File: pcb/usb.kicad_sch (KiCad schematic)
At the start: 9 parts, among them J3 918-418K2023S40001, U5 CH340N

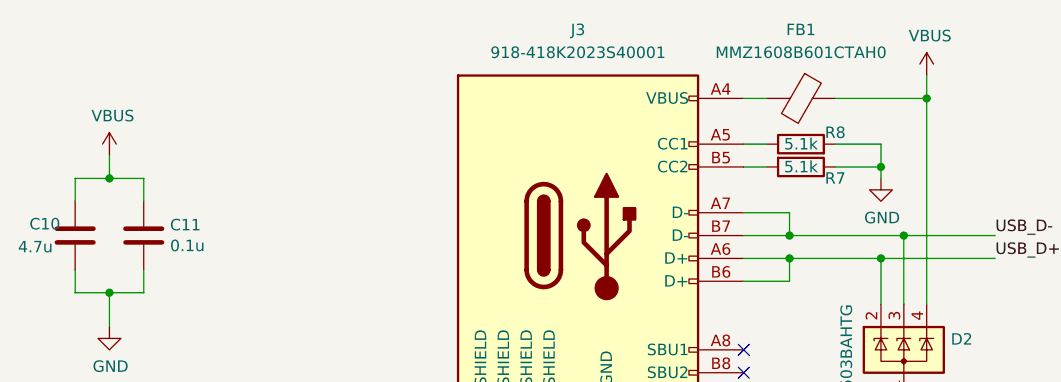
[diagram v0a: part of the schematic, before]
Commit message: Fix ERC warnings
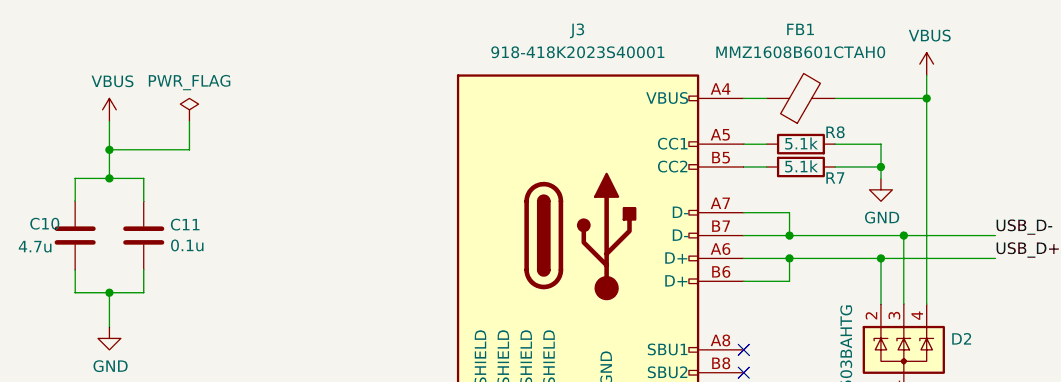
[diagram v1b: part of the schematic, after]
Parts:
- removed FB1: MMZ1608B601CTAH0, Capacitor_SMD:C_0603_1608Metric, symbol ultramote-rescue:Ferrite_Bead-Device
- added FB1: MMZ1608B601CTAH0, Capacitor_SMD:C_0603_1608Metric, symbol Device:FerriteBead
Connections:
- net VBUS: now also FB1.2
- net at J3.A4 (VBUS), J3.A9 (VBUS), J3.B4 (VBUS)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: now also FB1.1
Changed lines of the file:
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@@
   (junction (at 195.58 95.25) (diameter 0) (color 0 0 0 0)
+  )
+  (junction (at 59.055 66.675) (diameter 0) (color 0 0 0 0)
   )
   (junction (at 149.86 60.96) (diameter 0) (color 0 0 0 0)
@@
     (stroke (width 0) (type default) (color 0 0 0 0))
   )
-  (wire (pts (xy 59.055 67.31) (xy 59.055 69.85))
+  (wire (pts (xy 59.055 63.5) (xy 59.055 66.675))
     (stroke (width 0) (type default) (color 0 0 0 0))
   )
@@
     (stroke (width 0) (type default) (color 0 0 0 0))
   )
+  (wire (pts (xy 59.055 66.675) (xy 59.055 69.85))
+    (stroke (width 0) (type default) (color 0 0 0 0))
+  )
+  (wire (pts (xy 67.945 66.675) (xy 59.055 66.675))
+    (stroke (width 0) (type default) (color 0 0 0 0))
+  )
   (wire (pts (xy 185.42 82.55) (xy 182.88 82.55))
     (stroke (width 0) (type default) (color 0 0 0 0))
@@
   )
   (wire (pts (xy 134.62 73.66) (xy 134.62 76.2))
+    (stroke (width 0) (type default) (color 0 0 0 0))
+  )
+  (wire (pts (xy 67.945 63.5) (xy 67.945 66.675))
     (stroke (width 0) (type default) (color 0 0 0 0))
   )
@@
     (pin "1")
   )
-  (symbol (lib_id "ultramote-rescue:Ferrite_Bead-Device") (at 135.89 60.96 270) (unit 1)
-    (in_bom yes) (on_board yes)
-    (property "Reference" "FB1" (id 0) (at 135.89 53.34 90))
-    (property "Value" "MMZ1608B601CTAH0" (id 1) (at 135.89 55.88 90))
-    (property "Footprint" "Capacitor_SMD:C_0603_1608Metric" (id 2) (at 135.89 59.182 90)
-      (effects (font (size 1.27 1.27)) hide)
-    )
-    (property "Datasheet" "~" (id 3) (at 135.89 60.96 0)
-      (effects (font (size 1.27 1.27)) hide)
-    )
-    (property "LCSC Part Number" "C97120" (id 4) (at 135.89 60.96 0)
-      (effects (font (size 1.27 1.27)) hide)
-    )
-    (property "Manufacturer Part Number" "MMZ1608B601CTAH0" (id 5) (at 135.89 60.96 0)
-      (effects (font (size 1.27 1.27)) hide)
-    )
-    (pin "1")
-    (pin "2")
-  )
   (symbol (lib_id "Device:C") (at 62.865 76.2 0) (unit 1)
     (in_bom yes) (on_board yes)
@@
     (pin "2")
   )
-  (symbol (lib_id "power:VBUS") (at 59.055 67.31 0) (unit 1)
-    (in_bom yes) (on_board yes)
-    (property "Reference" "#PWR033" (id 0) (at 59.055 71.12 0)
-      (effects (font (size 1.27 1.27)) hide)
-    )
-    (property "Value" "VBUS" (id 1) (at 59.436 62.9158 0))
-    (property "Footprint" "" (id 2) (at 59.055 67.31 0)
-      (effects (font (size 1.27 1.27)) hide)
-    )
-    (property "Datasheet" "" (id 3) (at 59.055 67.31 0)
+  (symbol (lib_id "power:VBUS") (at 59.055 63.5 0) (unit 1)
+    (in_bom yes) (on_board yes)
+    (property "Reference" "#PWR033" (id 0) (at 59.055 67.31 0)
+      (effects (font (size 1.27 1.27)) hide)
+    )
+    (property "Value" "VBUS" (id 1) (at 59.436 59.1058 0))
+    (property "Footprint" "" (id 2) (at 59.055 63.5 0)
+      (effects (font (size 1.27 1.27)) hide)
+    )
+    (property "Datasheet" "" (id 3) (at 59.055 63.5 0)
       (effects (font (size 1.27 1.27)) hide)
     )
@@
     )
     (property "Datasheet" "" (id 3) (at 149.86 58.42 0)
+      (effects (font (size 1.27 1.27)) hide)
+    )
+    (pin "1")
+  )
+  (symbol (lib_id "power:PWR_FLAG") (at 67.945 63.5 0) (unit 1)
+    (in_bom yes) (on_board yes)
+    (property "Reference" "#FLG0102" (id 0) (at 67.945 61.595 0)
+      (effects (font (size 1.27 1.27)) hide)
+    )
+    (property "Value" "PWR_FLAG" (id 1) (at 67.945 59.055 0))
+    (property "Footprint" "" (id 2) (at 67.945 63.5 0)
+      (effects (font (size 1.27 1.27)) hide)
+    )
+    (property "Datasheet" "~" (id 3) (at 67.945 63.5 0)
       (effects (font (size 1.27 1.27)) hide)
     )
@@
       (effects (font (size 1.27 1.27)) hide)
     )
+    (pin "1")
+    (pin "2")
+  )
+  (symbol (lib_id "Device:FerriteBead") (at 135.89 60.96 90) (unit 1)
+    (in_bom yes) (on_board yes) (fields_autoplaced)
+    (property "Reference" "FB1" (id 0) (at 135.8392 53.34 90))
+    (property "Value" "MMZ1608B601CTAH0" (id 1) (at 135.8392 55.88 90))
+    (property "Footprint" "Capacitor_SMD:C_0603_1608Metric" (id 2) (at 135.89 62.738 90)
+      (effects (font (size 1.27 1.27)) hide)
+    )
+    (property "Datasheet" "~" (id 3) (at 135.89 60.96 0)
+      (effects (font (size 1.27 1.27)) hide)
+    )
+    (property "LCSC Part Number" "C97120" (id 4) (at 135.89 60.96 0)
+      (effects (font (size 1.27 1.27)) hide)
+    )
+    (property "Manufacturer Part Number" "MMZ1608B601CTAH0" (id 5) (at 135.89 60.96 0)
+      (effects (font (size 1.27 1.27)) hide)
+    )

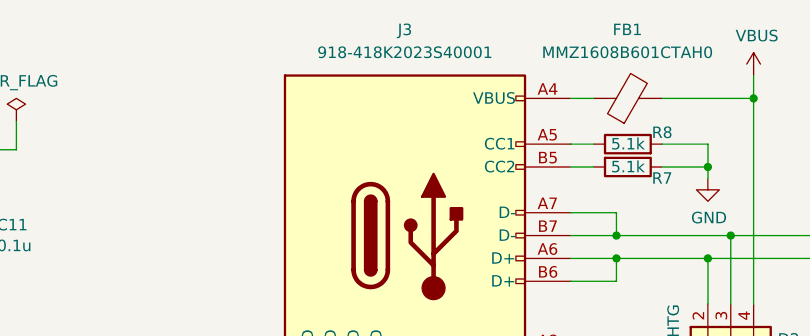
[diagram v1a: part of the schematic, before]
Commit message: Add datasheet links
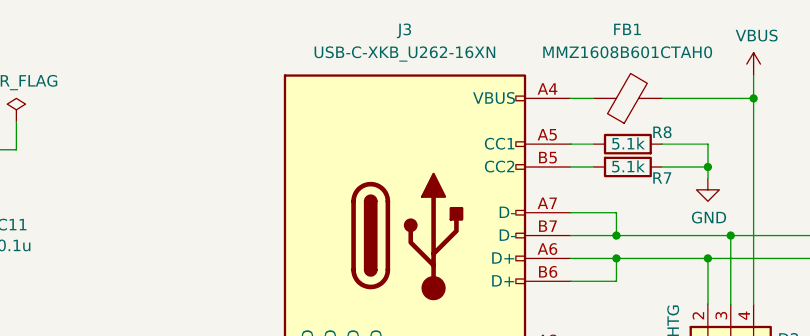
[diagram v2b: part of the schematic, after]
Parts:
- J3: value 918-418K2023S40001 -> USB-C-XKB_U262-16XN
- U5: LCSC Part Number C2977777 -> C2977777
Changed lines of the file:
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@@
       (effects (font (size 1.27 1.27)) hide)
     )
-    (property "Datasheet" "" (id 3) (at 195.58 82.55 0)
-      (effects (font (size 1.27 1.27)) hide)
-    )
-    (property "LCSC Part Number" " C2977777 " (id 4) (at 195.58 82.55 0)
+    (property "Datasheet" "https://datasheet.lcsc.com/lcsc/2202231130_WCH-Jiangsu-Qin-Heng-CH340N_C2977777.pdf" (id 3) (at 195.58 82.55 0)
+      (effects (font (size 1.27 1.27)) hide)
+    )
+    (property "LCSC Part Number" "C2977777" (id 4) (at 195.58 82.55 0)
       (effects (font (size 1.27 1.27)) hide)
     )
@@
     (in_bom yes) (on_board yes) (fields_autoplaced)
     (property "Reference" "J3" (id 0) (at 111.125 53.34 0))
-    (property "Value" "918-418K2023S40001" (id 1) (at 111.125 55.88 0))
+    (property "Value" "USB-C-XKB_U262-16XN" (id 1) (at 111.125 55.88 0))
     (property "Footprint" "ultramote:USB_C_Receptacle_XKB_U262-16XN-4BVC11" (id 2) (at 118.11 76.2 0)
       (effects (font (size 1.27 1.27)) hide)
     )
-    (property "Datasheet" "https://www.usb.org/sites/default/files/documents/usb_type-c.zip" (id 3) (at 114.3 106.68 0)
-      (effects (font (size 1.27 1.27)) hide)
-    )
+    (property "Datasheet" "https://datasheet.lcsc.com/lcsc/2103051833_Jing-Extension-of-the-Electronic-Co--918-418K2023S40001_C167321.pdf" (id 3) (at 114.3 106.68 0)
+      (effects (font (size 1.27 1.27)) hide)
+    )

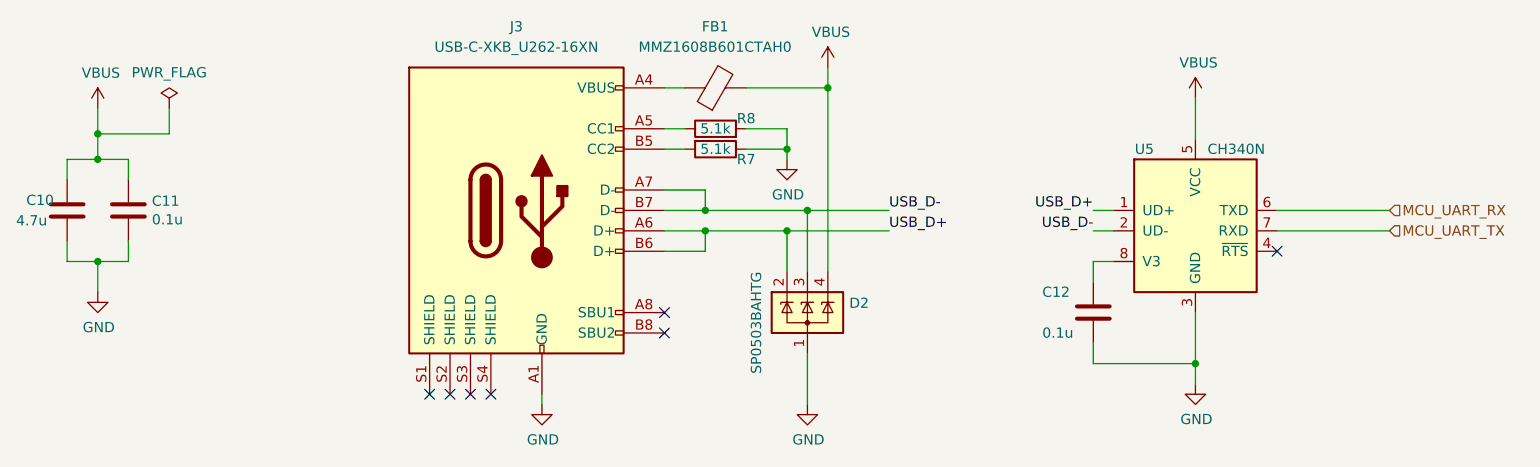
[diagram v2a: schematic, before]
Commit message: Migrate project to KiCad v7
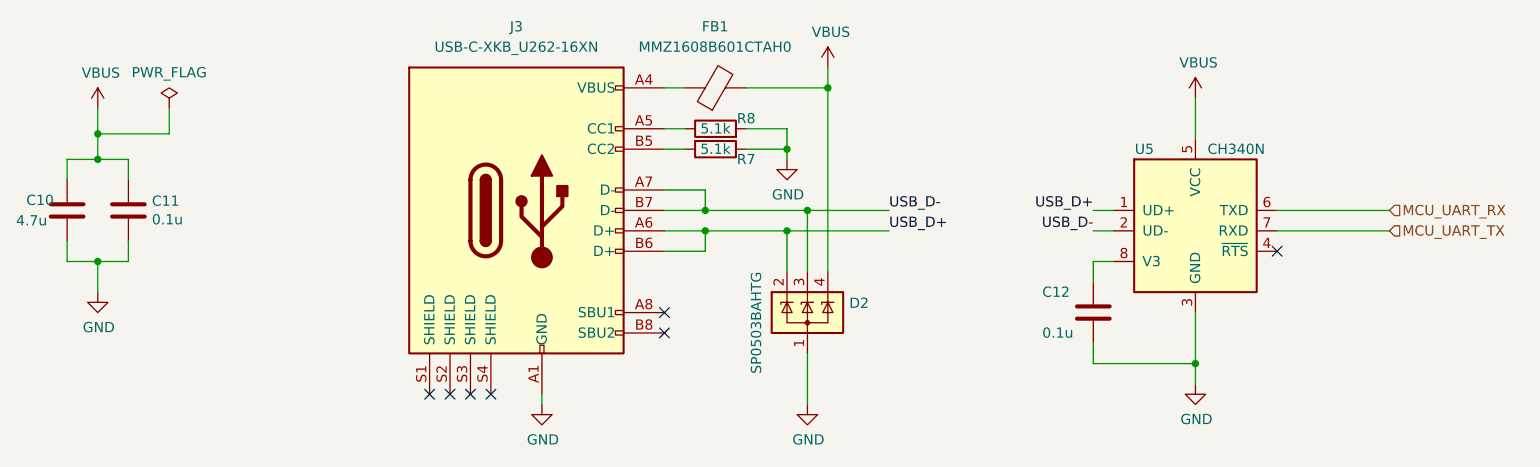
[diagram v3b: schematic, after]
